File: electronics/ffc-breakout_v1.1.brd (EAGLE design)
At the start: 25.4 x 22.9 mm, 3 parts, among them X2 AMP_SFW16R-2STE1LF

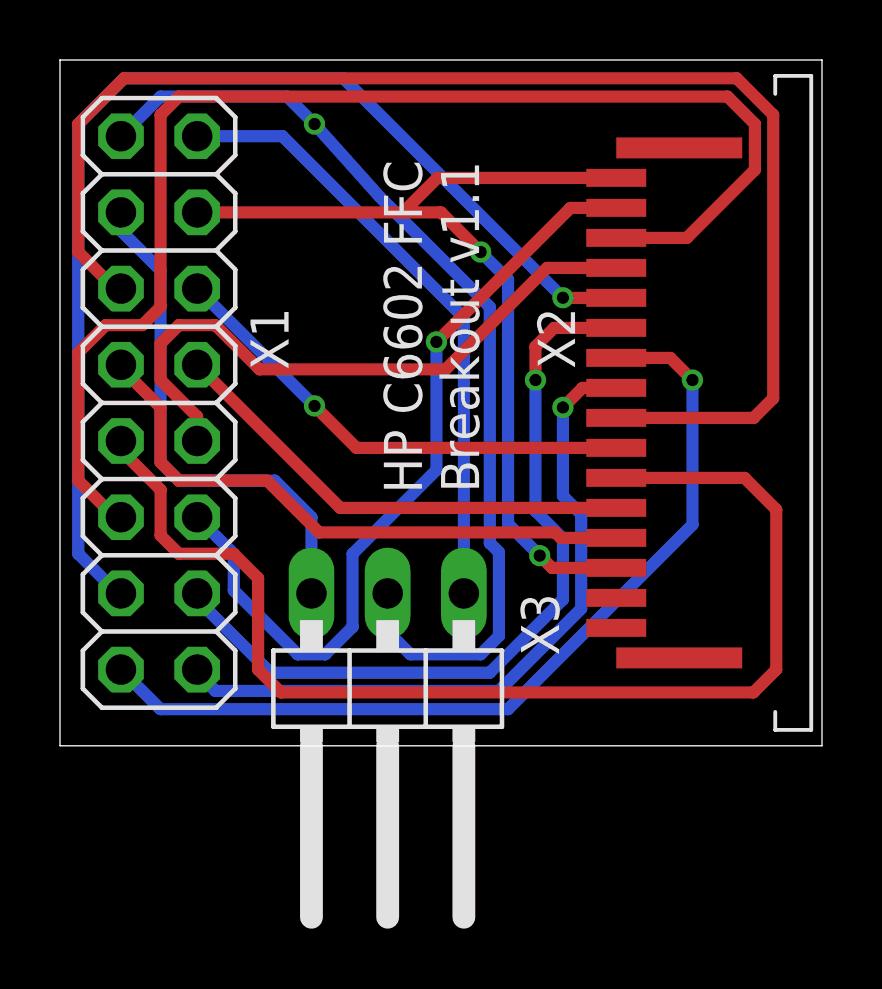
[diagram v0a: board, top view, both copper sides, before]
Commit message: Electronics v1.1 draft updates
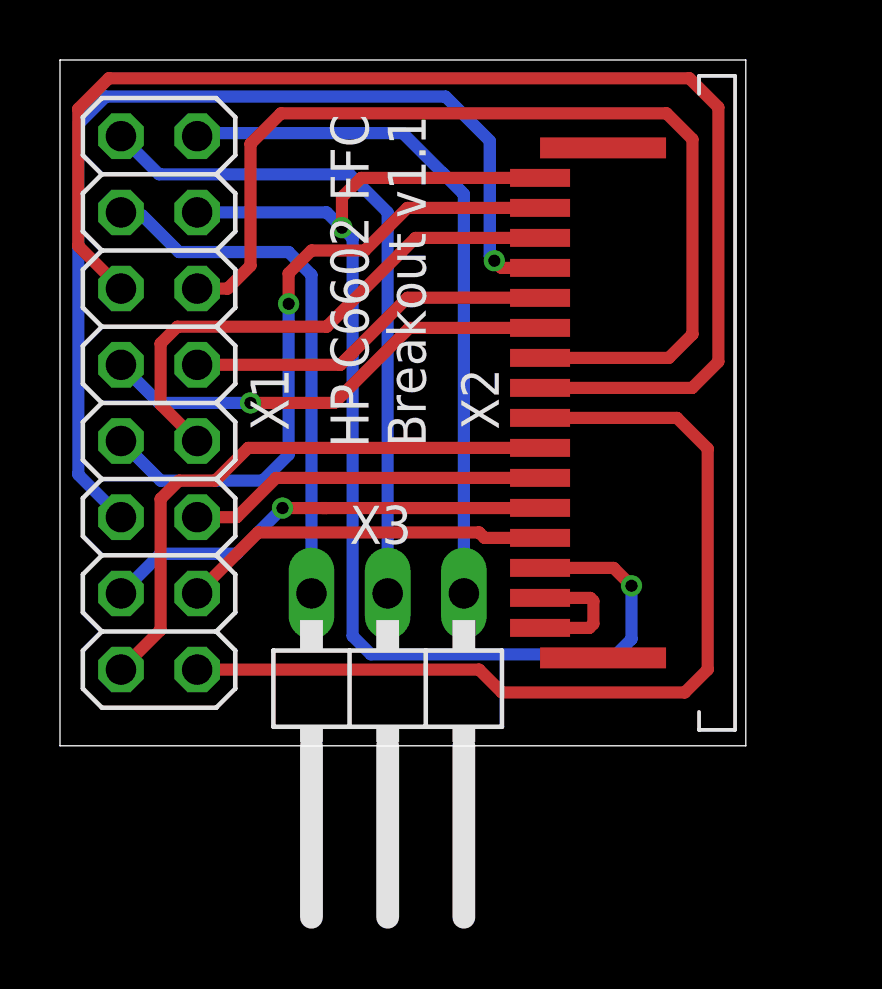
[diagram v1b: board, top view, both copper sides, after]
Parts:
- moved X2 2.54 mm to (16.0, 11.4)
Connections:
- removed net N$18: X1.12, X2.P$8
- new net N$5: X2.P$1, X2.P$2
- new net N$7: X1.2, X2.P$7
- net N$10: now also X1.5, X2.P$6; no longer X1.4, X2.P$12
- net N$11: now also X1.6, X2.P$13; no longer X1.5, X2.P$15
- net N$12: now also X1.7; no longer X1.6
- net N$13: now also X1.8, X2.P$15; no longer X1.7, X2.P$13
- net N$14: now also X1.9, X2.P$12; no longer X1.8, X2.P$6
- net N$15: now also X1.10, X2.P$11; no longer X1.9, X2.P$5
- net N$16: now also X1.11, X2.P$10; no longer X1.10, X2.P$4
- net N$17: now also X1.12, X2.P$9; no longer X1.11, X2.P$7
- net N$6: now also X2.P$8; no longer X2.P$9
- net N$8: now also X1.3, X2.P$4; no longer X1.2, X2.P$10
- net N$9: now also X1.4, X2.P$5; no longer X1.3, X2.P$11
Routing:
- net N$18: track 45.4 -> 0.00 mm
- net N$17: track 16.2 -> 43.5 mm, vias 1 -> 0
- net N$14: track 39.6 -> 12.8 mm
- net N$10: track 37.9 -> 12.0 mm, vias 1 -> 0
- net N$12: track 43.5 -> 17.9 mm
- net N$7: track 0.00 -> 19.6 mm
- net N$8: track 29.8 -> 12.3 mm, vias 1 -> 0
- net N$16: track 20.0 -> 33.6 mm
- net N$9: track 26.2 -> 15.3 mm
- net N$3: track 31.2 -> 41.5 mm
- net N$1: track 32.5 -> 22.6 mm, vias 1 -> 0
- net N$6: track 23.3 -> 31.0 mm, vias 1 -> 0
- net N$11: track 26.7 -> 34.1 mm
- net N$5: track 0.00 -> 4.42 mm
- net N$2: track 20.6 -> 24.1 mm
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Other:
- board size 25.4 x 22.9 mm -> 22.9 x 22.9 mm
